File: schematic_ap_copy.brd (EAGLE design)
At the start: 47 x 28 mm, 47 parts, among them J1 FTDI_DEVICE, M1 WIRELESS-NRF24L01, U1 ATMEGA328P_TQFP, U2 GY-521MPU6050

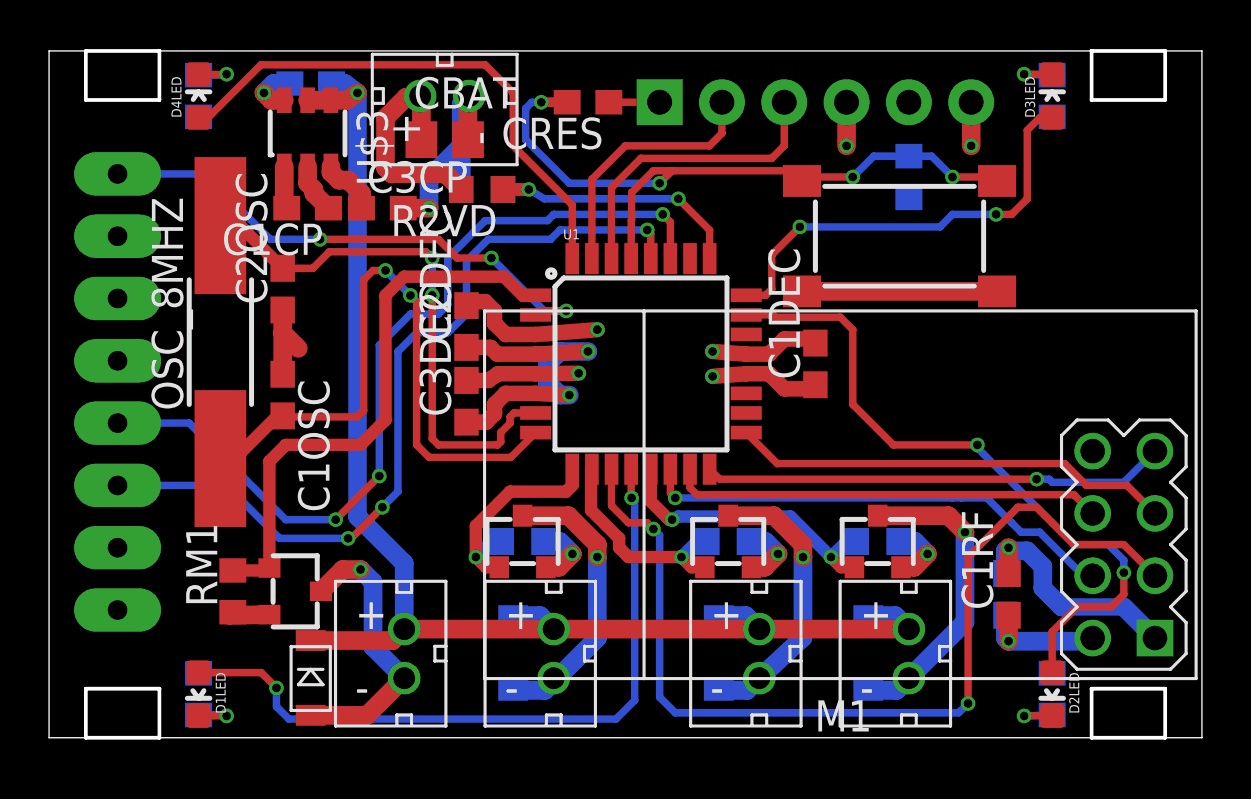
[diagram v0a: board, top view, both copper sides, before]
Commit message: Pre-Ground Changes
Seperating the grounds on the motor drivers
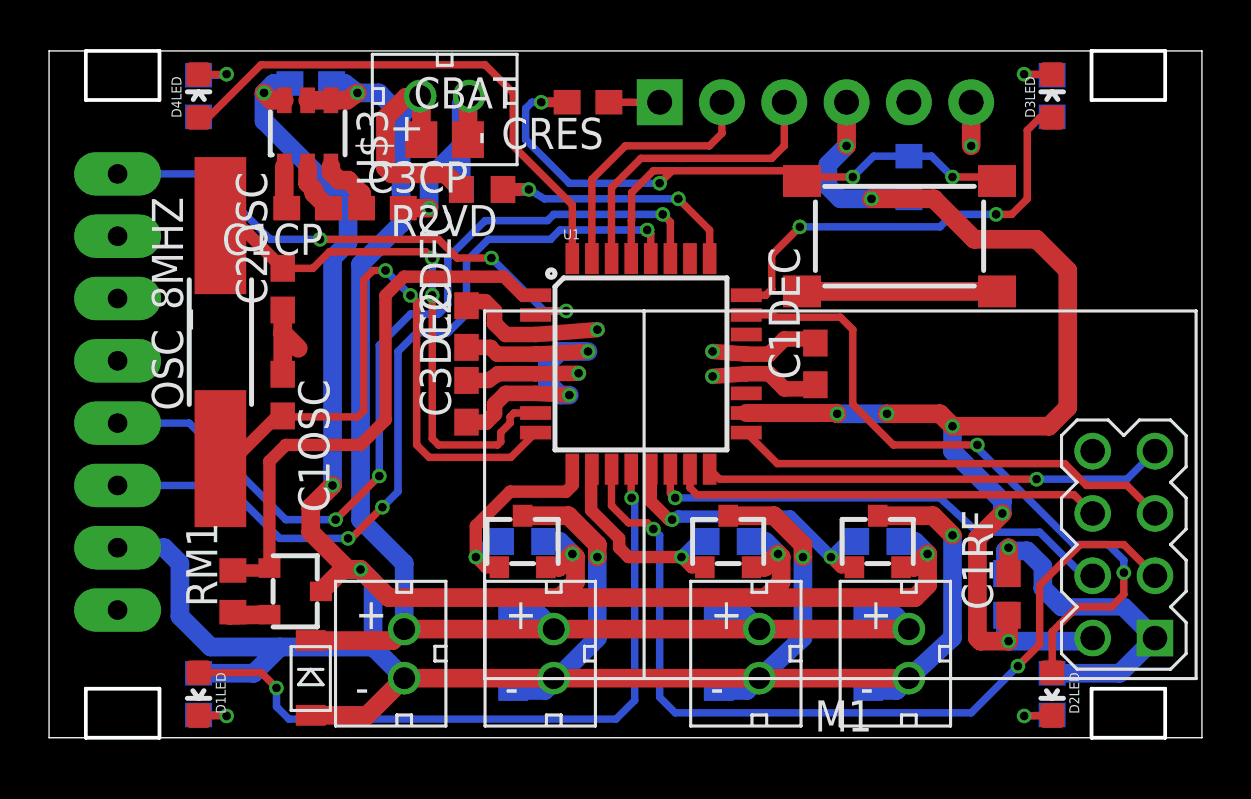
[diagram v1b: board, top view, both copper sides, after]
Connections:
- removed net N$15: DM1.POS, U$1.3, U$4.-
- removed net N$20: DM2.POS, U$2.3, U$5.-
- removed net N$24: DM3.POS, U$6.3, U$7.-
- removed net N$26: DM4.POS, U$8.3, U$9.-
- net GND: now also DM1.POS, DM2.POS, DM3.POS, DM4.POS, U$1.3, U$2.3, U$4.-, U$5.-, U$6.3, U$7.-, U$8.3, U$9.-
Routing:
- net GND: track 57.6 -> 198.8 mm, vias 10 -> 15
- net 3V3: track 27.2 -> 72.3 mm, vias 4 -> 9
- net N$26: track 12.6 -> 0.00 mm, vias 1 -> 0
- net N$20: track 11.8 -> 0.00 mm, vias 1 -> 0
- net N$24: track 11.6 -> 0.00 mm, vias 1 -> 0
- net N$15: track 11.6 -> 0.00 mm, vias 1 -> 0
- net CE: track 39.1 -> 35.8 mm
- net VBAT: track 65.3 -> 68.2 mm

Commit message: Pre-Polygons
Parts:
- moved CBAT 1.27 mm to (17.4, 24.4)
- moved U$11 1.27 mm to (17.4, 26.2)
- moved R1VD 0.76 mm to (18.4, 22.4)
- moved R2VD 0.76 mm to (18.4, 22.4)
- moved CRES 0.51 mm to (22.5, 25.9), turned to 270 degrees
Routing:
- net GND: track 198.8 -> 286.4 mm, vias 15 -> 24
- net 3V3: track 72.3 -> 121.9 mm, vias 9 -> 14
- net TOSC2: track 27.0 -> 17.5 mm
- net RESET: track 28.7 -> 23.7 mm
- net INT: track 21.9 -> 20.1 mm
- net LED4: track 21.9 -> 23.7 mm
- net PWM1: track 23.1 -> 24.2 mm, vias 0 -> 2
- net TOSC1: track 22.3 -> 21.3 mm, vias 2 -> 4
- net VBAT: track 68.2 -> 69.1 mm
- net VDIV: track 11.3 -> 10.6 mm
- net N$3: track 2.07 -> 2.77 mm

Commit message: First Draft
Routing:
- net 3V3: track 121.9 -> 120.4 mm
- added copper zone on layer 1, net 3V3
- added copper zone on layer 16, net 3V3
- added copper zone on layer 1, net GND
- added copper zone on layer 16, net GND
- added copper zone on layer 1, net VBAT
